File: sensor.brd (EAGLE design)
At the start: 76 x 50 mm, 38 parts, among them U2 MCP73831, U3 BMP180, U4 TSL2561, U6 TPS63001DRCR, Y1 12mhz

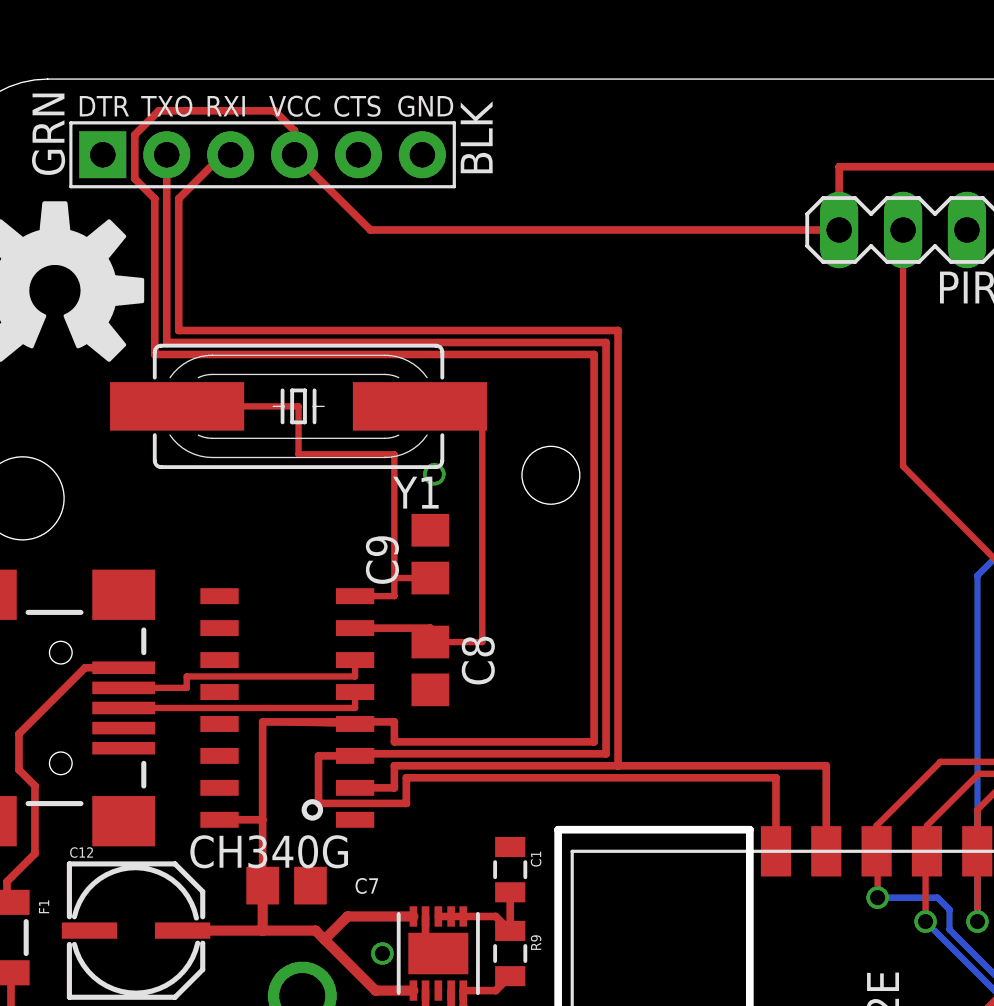
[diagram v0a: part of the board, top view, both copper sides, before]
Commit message: Tart the PCB up a bit, nice 45 degree bends. Add a 0.1uf cap across the PIR sensor.
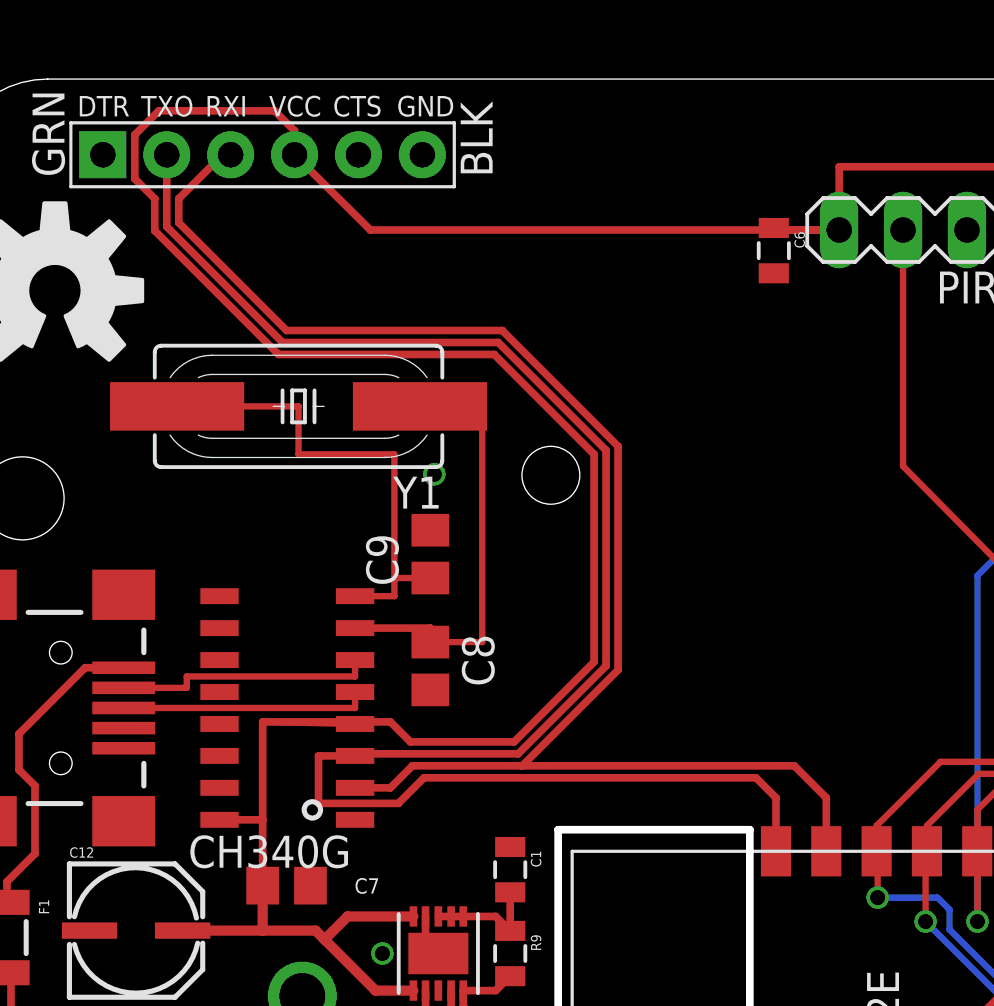
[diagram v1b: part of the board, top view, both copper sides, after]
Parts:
- added C6: 0.1uf, SparkFun-Capacitors:0805
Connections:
- net 3.3V: now also C6.1
- net GND: now also C6.2
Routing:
- net TX: track 76.8 -> 68.5 mm
- net 3.3V: track 259.3 -> 254.3 mm
- net RX: track 65.8 -> 60.9 mm
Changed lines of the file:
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@@
 <attribute name="PROD_ID" value="CONN-09696" x="53" y="8" size="0.6096" layer="27" rot="R90" display="off"/>
 </element>
+<element name="C6" library="SparkFun-Capacitors" package="0805" value="0.1uf" x="32.86125" y="43.18" rot="R270"/>
 </elements>
 <signals>
@@
 <wire x1="13.81125" y1="46.99" x2="16.8275" y2="44" width="0.3048" layer="1"/>
 <wire x1="16.8275" y1="44" x2="35.46" y2="44" width="0.3048" layer="1"/>
-<wire x1="12.54375" y1="24.4475" x2="17.78" y2="24.4475" width="0.3048" layer="1"/>
-<wire x1="17.78" y1="24.4475" x2="17.78" y2="23.65375" width="0.3048" layer="1"/>
-<wire x1="17.78" y1="23.65375" x2="25.7175" y2="23.65375" width="0.3048" layer="1"/>
-<wire x1="25.7175" y1="23.65375" x2="25.7175" y2="39.0525" width="0.3048" layer="1"/>
-<wire x1="25.7175" y1="39.0525" x2="8.255" y2="39.0525" width="0.3048" layer="1"/>
-<wire x1="8.255" y1="39.0525" x2="8.255" y2="45.24375" width="0.3048" layer="1"/>
+<wire x1="12.54375" y1="24.4475" x2="17.62125" y2="24.4475" width="0.3048" layer="1"/>
+<wire x1="17.62125" y1="24.4475" x2="18.415" y2="23.65375" width="0.3048" layer="1"/>
+<wire x1="18.415" y1="23.65375" x2="22.5425" y2="23.65375" width="0.3048" layer="1"/>
 <wire x1="8.255" y1="45.24375" x2="7.46125" y2="46.0375" width="0.3048" layer="1"/>
 <wire x1="7.46125" y1="46.0375" x2="7.46125" y2="47.78375" width="0.3048" layer="1"/>
@@
 <wire x1="58.7375" y1="18.57375" x2="71.17325" y2="18.57375" width="0.3048" layer="1"/>
 <wire x1="71.17325" y1="18.57375" x2="74.127" y2="15.62" width="0.3048" layer="1"/>
+<wire x1="21.74875" y1="39.0525" x2="25.7175" y2="35.08375" width="0.3048" layer="1"/>
+<wire x1="25.7175" y1="35.08375" x2="25.7175" y2="26.82875" width="0.3048" layer="1"/>
+<wire x1="25.7175" y1="26.82875" x2="22.5425" y2="23.65375" width="0.3048" layer="1"/>
+<wire x1="21.74875" y1="39.0525" x2="13.17625" y2="39.0525" width="0.3048" layer="1"/>
+<wire x1="13.17625" y1="39.0525" x2="8.255" y2="43.97375" width="0.3048" layer="1"/>
+<wire x1="8.255" y1="43.97375" x2="8.255" y2="45.24375" width="0.3048" layer="1"/>
+<contactref element="C6" pad="1"/>
+<wire x1="32.86125" y1="44.08" x2="33.17875" y2="44" width="0.3048" layer="1"/>
+<wire x1="33.17875" y1="44" x2="35.46" y2="44" width="0.3048" layer="1"/>
 </signal>
 <signal name="GND">
@@
 <via x="50.95875" y="20.47875" extent="1-16" drill="0.6"/>
 <via x="56.1975" y="13.97" extent="1-16" drill="0.6"/>
+<contactref element="C6" pad="2"/>
 </signal>
 <signal name="TX">
@@
 <wire x1="16.21875" y1="23.095" x2="14.76375" y2="23.095" width="0.3048" layer="1"/>
 <wire x1="14.76375" y1="23.095" x2="14.76375" y2="21.2075" width="0.3048" layer="1"/>
-<wire x1="14.76375" y1="21.2075" x2="18.25625" y2="21.2075" width="0.3048" layer="1"/>
-<wire x1="18.25625" y1="21.2075" x2="18.25625" y2="22.225" width="0.3048" layer="1"/>
-<wire x1="18.25625" y1="22.225" x2="32.9475" y2="22.225" width="0.3048" layer="1"/>
-<wire x1="32.9475" y1="22.225" x2="32.9475" y2="19.30375" width="0.3048" layer="1"/>
-<wire x1="8.73125" y1="46.99" x2="8.73125" y2="39.52875" width="0.3048" layer="1"/>
-<wire x1="8.73125" y1="39.52875" x2="26.19375" y2="39.52875" width="0.3048" layer="1"/>
-<wire x1="26.19375" y1="39.52875" x2="26.19375" y2="23.1775" width="0.3048" layer="1"/>
-<wire x1="26.19375" y1="23.1775" x2="16.21875" y2="23.1775" width="0.3048" layer="1"/>
+<wire x1="14.76375" y1="21.2075" x2="17.93875" y2="21.2075" width="0.3048" layer="1"/>
 <wire x1="16.21875" y1="23.1775" x2="16.21875" y2="23.095" width="0.3048" layer="1"/>
+<wire x1="17.93875" y1="21.2075" x2="18.95625" y2="22.225" width="0.3048" layer="1"/>
+<wire x1="32.9475" y1="19.30375" x2="32.9475" y2="21.43125" width="0.3048" layer="1"/>
+<wire x1="32.9475" y1="21.43125" x2="32.15375" y2="22.225" width="0.3048" layer="1"/>
+<wire x1="32.15375" y1="22.225" x2="18.95625" y2="22.225" width="0.3048" layer="1"/>
+<wire x1="21.9075" y1="39.52875" x2="26.19375" y2="35.2425" width="0.3048" layer="1"/>
+<wire x1="26.19375" y1="35.2425" x2="26.19375" y2="26.67" width="0.3048" layer="1"/>
+<wire x1="26.19375" y1="26.67" x2="22.70125" y2="23.1775" width="0.3048" layer="1"/>
+<wire x1="16.21875" y1="23.1775" x2="22.70125" y2="23.1775" width="0.3048" layer="1"/>
+<wire x1="8.73125" y1="46.99" x2="8.73125" y2="44.1325" width="0.3048" layer="1"/>
+<wire x1="8.73125" y1="44.1325" x2="13.335" y2="39.52875" width="0.3048" layer="1"/>
+<wire x1="13.335" y1="39.52875" x2="21.9075" y2="39.52875" width="0.3048" layer="1"/>
 </signal>
 <signal name="RX">
@@
 <contactref element="JP2" pad="P$3"/>
 <contactref element="U$11" pad="2"/>
-<wire x1="16.21875" y1="21.825" x2="17.78" y2="21.825" width="0.3048" layer="1"/>
-<wire x1="17.78" y1="21.825" x2="17.78" y2="22.70125" width="0.3048" layer="1"/>
-<wire x1="17.78" y1="22.70125" x2="26.67" y2="22.70125" width="0.3048" layer="1"/>
-<wire x1="26.67" y1="22.70125" x2="34.9475" y2="22.70125" width="0.3048" layer="1"/>
-<wire x1="34.9475" y1="22.70125" x2="34.9475" y2="19.30375" width="0.3048" layer="1"/>
+<wire x1="16.21875" y1="21.825" x2="17.62125" y2="21.825" width="0.3048" layer="1"/>
 <wire x1="11.27125" y1="46.99" x2="10.95375" y2="46.99" width="0.3048" layer="1"/>
 <wire x1="10.95375" y1="46.99" x2="9.2075" y2="45.24375" width="0.3048" layer="1"/>
-<wire x1="9.2075" y1="45.24375" x2="9.2075" y2="40.005" width="0.3048" layer="1"/>
-<wire x1="9.2075" y1="40.005" x2="26.67" y2="40.005" width="0.3048" layer="1"/>
-<wire x1="26.67" y1="40.005" x2="26.67" y2="22.70125" width="0.3048" layer="1"/>
+<wire x1="17.62125" y1="21.825" x2="18.4975" y2="22.70125" width="0.3048" layer="1"/>
+<wire x1="18.4975" y1="22.70125" x2="22.86" y2="22.70125" width="0.3048" layer="1"/>
+<wire x1="22.86" y1="22.70125" x2="33.6775" y2="22.70125" width="0.3048" layer="1"/>
+<wire x1="34.9475" y1="19.30375" x2="34.9475" y2="21.43125" width="0.3048" layer="1"/>
+<wire x1="34.9475" y1="21.43125" x2="33.6775" y2="22.70125" width="0.3048" layer="1"/>
+<wire x1="22.06625" y1="40.005" x2="26.67" y2="35.40125" width="0.3048" layer="1"/>
+<wire x1="26.67" y1="35.40125" x2="26.67" y2="26.51125" width="0.3048" layer="1"/>
+<wire x1="26.67" y1="26.51125" x2="22.86" y2="22.70125" width="0.3048" layer="1"/>
+<wire x1="9.2075" y1="45.24375" x2="9.2075" y2="44.29125" width="0.3048" layer="1"/>
+<wire x1="9.2075" y1="44.29125" x2="13.49375" y2="40.005" width="0.3048" layer="1"/>
+<wire x1="13.49375" y1="40.005" x2="22.06625" y2="40.005" width="0.3048" layer="1"/>
 </signal>
 <signal name="SDA">
